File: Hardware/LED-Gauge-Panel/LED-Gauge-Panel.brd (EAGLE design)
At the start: 35.5 x 42.9 mm, 3 parts

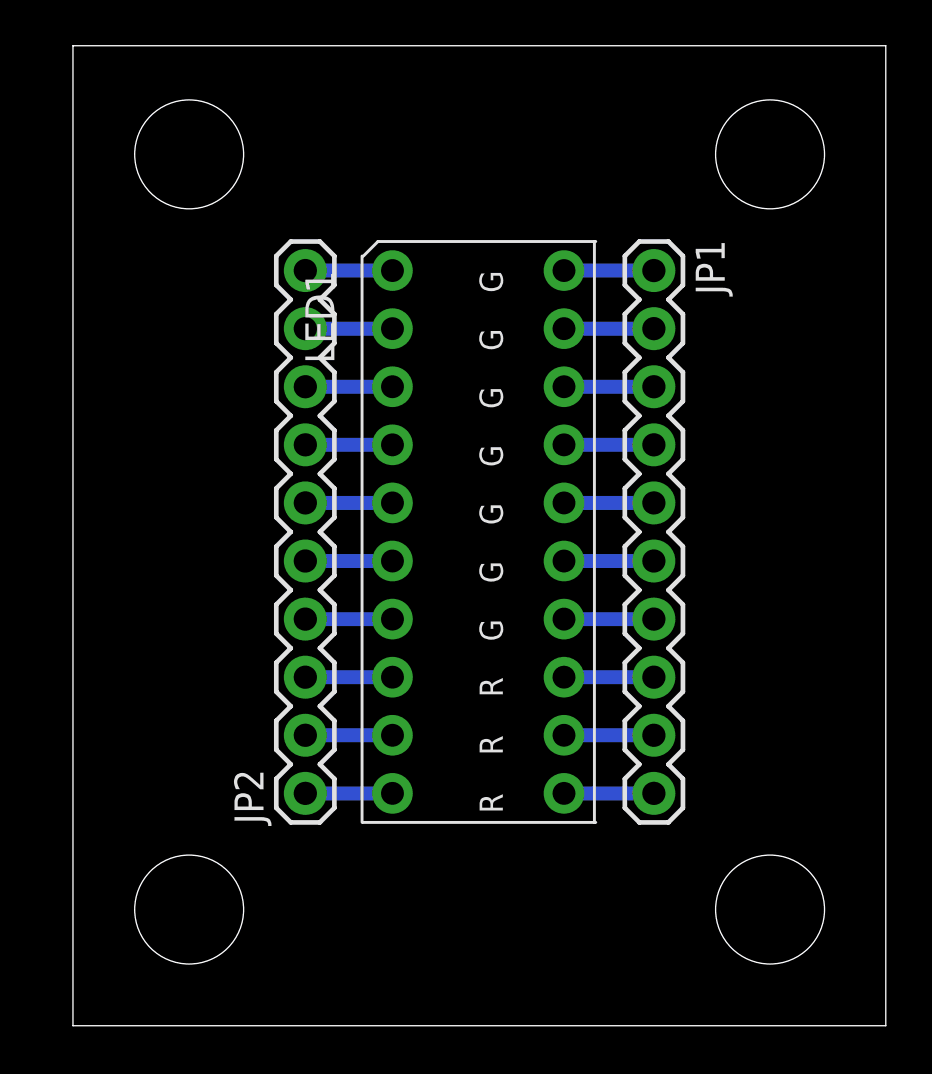
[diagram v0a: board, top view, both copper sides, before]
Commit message: Made the LED bargraph PCB smaller, added hole for on/off switch mounting
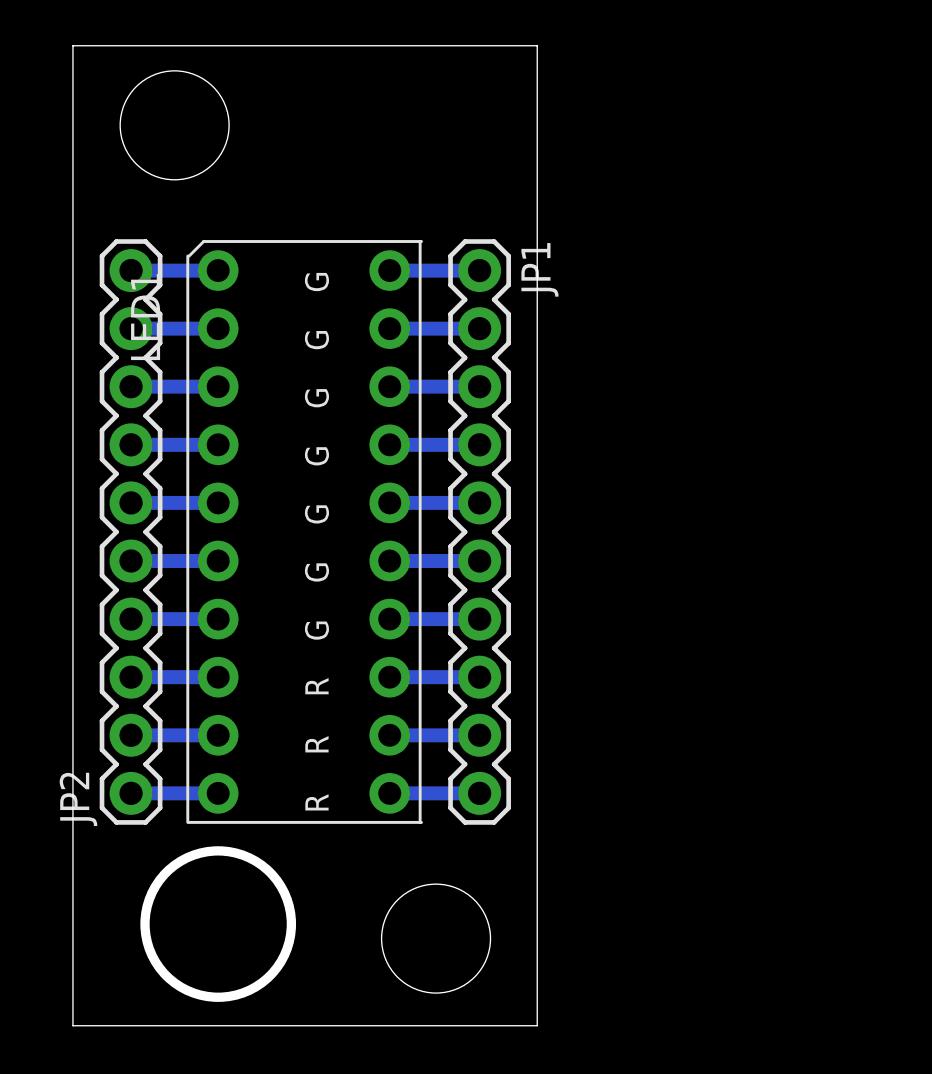
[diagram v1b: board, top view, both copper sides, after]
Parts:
- moved LED1 7.62 mm to (6.35, 33.0)
- moved JP2 7.62 mm to (2.54, 10.2)
- moved JP1 7.62 mm to (17.8, 33.0)
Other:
- board size 35.5 x 42.9 mm -> 20.3 x 42.9 mm
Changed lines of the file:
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@@
 <board>
 <plain>
-<wire x1="0" y1="0" x2="35.54" y2="0" width="0" layer="20"/>
-<wire x1="35.54" y1="0" x2="35.54" y2="42.85" width="0" layer="20"/>
-<wire x1="35.54" y1="42.85" x2="0" y2="42.85" width="0" layer="20"/>
+<wire x1="0" y1="0" x2="20.3" y2="0" width="0" layer="20"/>
+<wire x1="20.3" y1="0" x2="20.3" y2="42.85" width="0" layer="20"/>
+<wire x1="20.3" y1="42.85" x2="0" y2="42.85" width="0" layer="20"/>
 <wire x1="0" y1="42.85" x2="0" y2="0" width="0" layer="20"/>
-<hole x="5.08" y="5.08" drill="4.7625"/>
-<hole x="30.48" y="5.08" drill="4.7625"/>
-<hole x="5.08" y="38.1" drill="4.7625"/>
-<hole x="30.48" y="38.1" drill="4.7625"/>
+<hole x="15.875" y="3.81" drill="4.7625"/>
+<hole x="4.445" y="39.37" drill="4.7625"/>
+<circle x="6.35" y="4.445" radius="3.2" width="0.4064" layer="20"/>
 </plain>
 <attributes>
@@
 </autorouter>
 <elements>
-<element name="JP1" library="SparkFun-Connectors" package="1X10" value="" x="25.4" y="33.02" rot="R270">
-<attribute name="PROD_ID" value="CONN-11563" x="8.89" y="-5.08" size="1.778" layer="27" rot="R270" display="off"/>
+<element name="JP1" library="SparkFun-Connectors" package="1X10" value="" x="17.78" y="33.02" rot="R270">
+<attribute name="PROD_ID" value="CONN-11563" x="1.27" y="-5.08" size="1.778" layer="27" rot="R270" display="off"/>
 </element>
-<element name="JP2" library="SparkFun-Connectors" package="1X10" value="" x="10.16" y="10.16" rot="R90">
-<attribute name="PROD_ID" value="CONN-11563" x="31.75" y="48.26" size="1.778" layer="27" rot="R90" display="off"/>
+<element name="JP2" library="SparkFun-Connectors" package="1X10" value="" x="2.54" y="10.16" rot="R90">
+<attribute name="PROD_ID" value="CONN-11563" x="24.13" y="48.26" size="1.778" layer="27" rot="R90" display="off"/>
 </element>
-<element name="LED1" library="2016PowerPackLibraries" package="LED-10" value="LED-DC7G3HWA" x="13.97" y="33.02" rot="R270"/>
+<element name="LED1" library="2016PowerPackLibraries" package="LED-10" value="LED-DC7G3HWA" x="6.35" y="33.02" rot="R270"/>
 </elements>
 <signals>
@@
 <contactref element="LED1" pad="P$20"/>
 <contactref element="JP1" pad="1"/>
-<wire x1="21.47" y1="33.02" x2="25.4" y2="33.02" width="0.6096" layer="16"/>
+<wire x1="13.85" y1="33.02" x2="17.78" y2="33.02" width="0.6096" layer="16"/>
 </signal>
 <signal name="N$2">
 <contactref element="LED1" pad="P$19"/>
 <contactref element="JP1" pad="2"/>
-<wire x1="21.47" y1="30.48" x2="25.4" y2="30.48" width="0.6096" layer="16"/>
+<wire x1="13.85" y1="30.48" x2="17.78" y2="30.48" width="0.6096" layer="16"/>
 </signal>
 <signal name="N$3">
 <contactref element="LED1" pad="P$18"/>
 <contactref element="JP1" pad="3"/>
-<wire x1="21.47" y1="27.94" x2="25.4" y2="27.94" width="0.6096" layer="16"/>
+<wire x1="13.85" y1="27.94" x2="17.78" y2="27.94" width="0.6096" layer="16"/>
 </signal>
 <signal name="N$4">
 <contactref element="LED1" pad="P$17"/>
 <contactref element="JP1" pad="4"/>
-<wire x1="21.47" y1="25.4" x2="25.4" y2="25.4" width="0.6096" layer="16"/>
+<wire x1="13.85" y1="25.4" x2="17.78" y2="25.4" width="0.6096" layer="16"/>
 </signal>
 <signal name="N$5">
 <contactref element="LED1" pad="P$16"/>
 <contactref element="JP1" pad="5"/>
-<wire x1="21.47" y1="22.86" x2="25.4" y2="22.86" width="0.6096" layer="16"/>
+<wire x1="13.85" y1="22.86" x2="17.78" y2="22.86" width="0.6096" layer="16"/>
 </signal>
 <signal name="N$6">
 <contactref element="LED1" pad="P$15"/>
 <contactref element="JP1" pad="6"/>
-<wire x1="21.47" y1="20.32" x2="25.4" y2="20.32" width="0.6096" layer="16"/>
+<wire x1="13.85" y1="20.32" x2="17.78" y2="20.32" width="0.6096" layer="16"/>
 </signal>
 <signal name="N$7">
 <contactref element="LED1" pad="P$14"/>
 <contactref element="JP1" pad="7"/>
-<wire x1="21.47" y1="17.78" x2="25.4" y2="17.78" width="0.6096" layer="16"/>
+<wire x1="13.85" y1="17.78" x2="17.78" y2="17.78" width="0.6096" layer="16"/>
 </signal>
 <signal name="N$8">
 <contactref element="LED1" pad="P$13"/>
 <contactref element="JP1" pad="8"/>
-<wire x1="21.47" y1="15.24" x2="25.4" y2="15.24" width="0.6096" layer="16"/>
+<wire x1="13.85" y1="15.24" x2="17.78" y2="15.24" width="0.6096" layer="16"/>
 </signal>
 <signal name="N$9">
 <contactref element="LED1" pad="P$12"/>
 <contactref element="JP1" pad="9"/>
-<wire x1="21.47" y1="12.7" x2="25.4" y2="12.7" width="0.6096" layer="16"/>
+<wire x1="13.85" y1="12.7" x2="17.78" y2="12.7" width="0.6096" layer="16"/>
 </signal>
 <signal name="N$10">
 <contactref element="JP1" pad="10"/>
 <contactref element="LED1" pad="P$11"/>
-<wire x1="21.47" y1="10.16" x2="25.4" y2="10.16" width="0.6096" layer="16"/>
+<wire x1="13.85" y1="10.16" x2="17.78" y2="10.16" width="0.6096" layer="16"/>
 </signal>
 <signal name="N$11">
 <contactref element="LED1" pad="P$1"/>
 <contactref element="JP2" pad="10"/>
-<wire x1="13.97" y1="33.02" x2="10.16" y2="33.02" width="0.6096" layer="16"/>
+<wire x1="6.35" y1="33.02" x2="2.54" y2="33.02" width="0.6096" layer="16"/>
 </signal>
 <signal name="N$12">
 <contactref element="JP2" pad="9"/>
 <contactref element="LED1" pad="P$2"/>
-<wire x1="13.97" y1="30.48" x2="10.16" y2="30.48" width="0.6096" layer="16"/>
+<wire x1="6.35" y1="30.48" x2="2.54" y2="30.48" width="0.6096" layer="16"/>
 </signal>
 <signal name="N$13">
 <contactref element="JP2" pad="8"/>
 <contactref element="LED1" pad="P$3"/>
-<wire x1="13.97" y1="27.94" x2="10.16" y2="27.94" width="0.6096" layer="16"/>
+<wire x1="6.35" y1="27.94" x2="2.54" y2="27.94" width="0.6096" layer="16"/>
 </signal>
 <signal name="N$14">
 <contactref element="JP2" pad="7"/>
 <contactref element="LED1" pad="P$4"/>
-<wire x1="13.97" y1="25.4" x2="10.16" y2="25.4" width="0.6096" layer="16"/>
+<wire x1="6.35" y1="25.4" x2="2.54" y2="25.4" width="0.6096" layer="16"/>
 </signal>
 <signal name="N$15">
 <contactref element="JP2" pad="6"/>
 <contactref element="LED1" pad="P$5"/>
-<wire x1="13.97" y1="22.86" x2="10.16" y2="22.86" width="0.6096" layer="16"/>
+<wire x1="6.35" y1="22.86" x2="2.54" y2="22.86" width="0.6096" layer="16"/>
 </signal>
 <signal name="N$16">
 <contactref element="JP2" pad="5"/>
 <contactref element="LED1" pad="P$6"/>
-<wire x1="13.97" y1="20.32" x2="10.16" y2="20.32" width="0.6096" layer="16"/>
+<wire x1="6.35" y1="20.32" x2="2.54" y2="20.32" width="0.6096" layer="16"/>
 </signal>
 <signal name="N$17">
 <contactref element="JP2" pad="4"/>
 <contactref element="LED1" pad="P$7"/>
-<wire x1="13.97" y1="17.78" x2="10.16" y2="17.78" width="0.6096" layer="16"/>
+<wire x1="6.35" y1="17.78" x2="2.54" y2="17.78" width="0.6096" layer="16"/>
 </signal>
 <signal name="N$18">
 <contactref element="JP2" pad="3"/>
 <contactref element="LED1" pad="P$8"/>
-<wire x1="13.97" y1="15.24" x2="10.16" y2="15.24" width="0.6096" layer="16"/>
+<wire x1="6.35" y1="15.24" x2="2.54" y2="15.24" width="0.6096" layer="16"/>
 </signal>
 <signal name="N$19">
 <contactref element="JP2" pad="2"/>
 <contactref element="LED1" pad="P$9"/>
-<wire x1="13.97" y1="12.7" x2="10.16" y2="12.7" width="0.6096" layer="16"/>
+<wire x1="6.35" y1="12.7" x2="2.54" y2="12.7" width="0.6096" layer="16"/>
 </signal>
 <signal name="N$20">
 <contactref element="JP2" pad="1"/>
 <contactref element="LED1" pad="P$10"/>
-<wire x1="13.97" y1="10.16" x2="10.16" y2="10.16" width="0.6096" layer="16"/>
+<wire x1="6.35" y1="10.16" x2="2.54" y2="10.16" width="0.6096" layer="16"/>
 </signal>
 </signals>
